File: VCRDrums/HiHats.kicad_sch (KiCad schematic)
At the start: 107 parts, among them Q601 BC847, Q602 BC857, Q603 BC847, Q604 BC857, Q605 BC847, Q606 BC847, Q607 BC847, Q608 BC847, Q609 BC847, Q610 BC847, Q611 BC847, Q612 BC847, Q613 BC847, Q614 BC847, Q615 BC857, U601 TL074, U602 LM13700

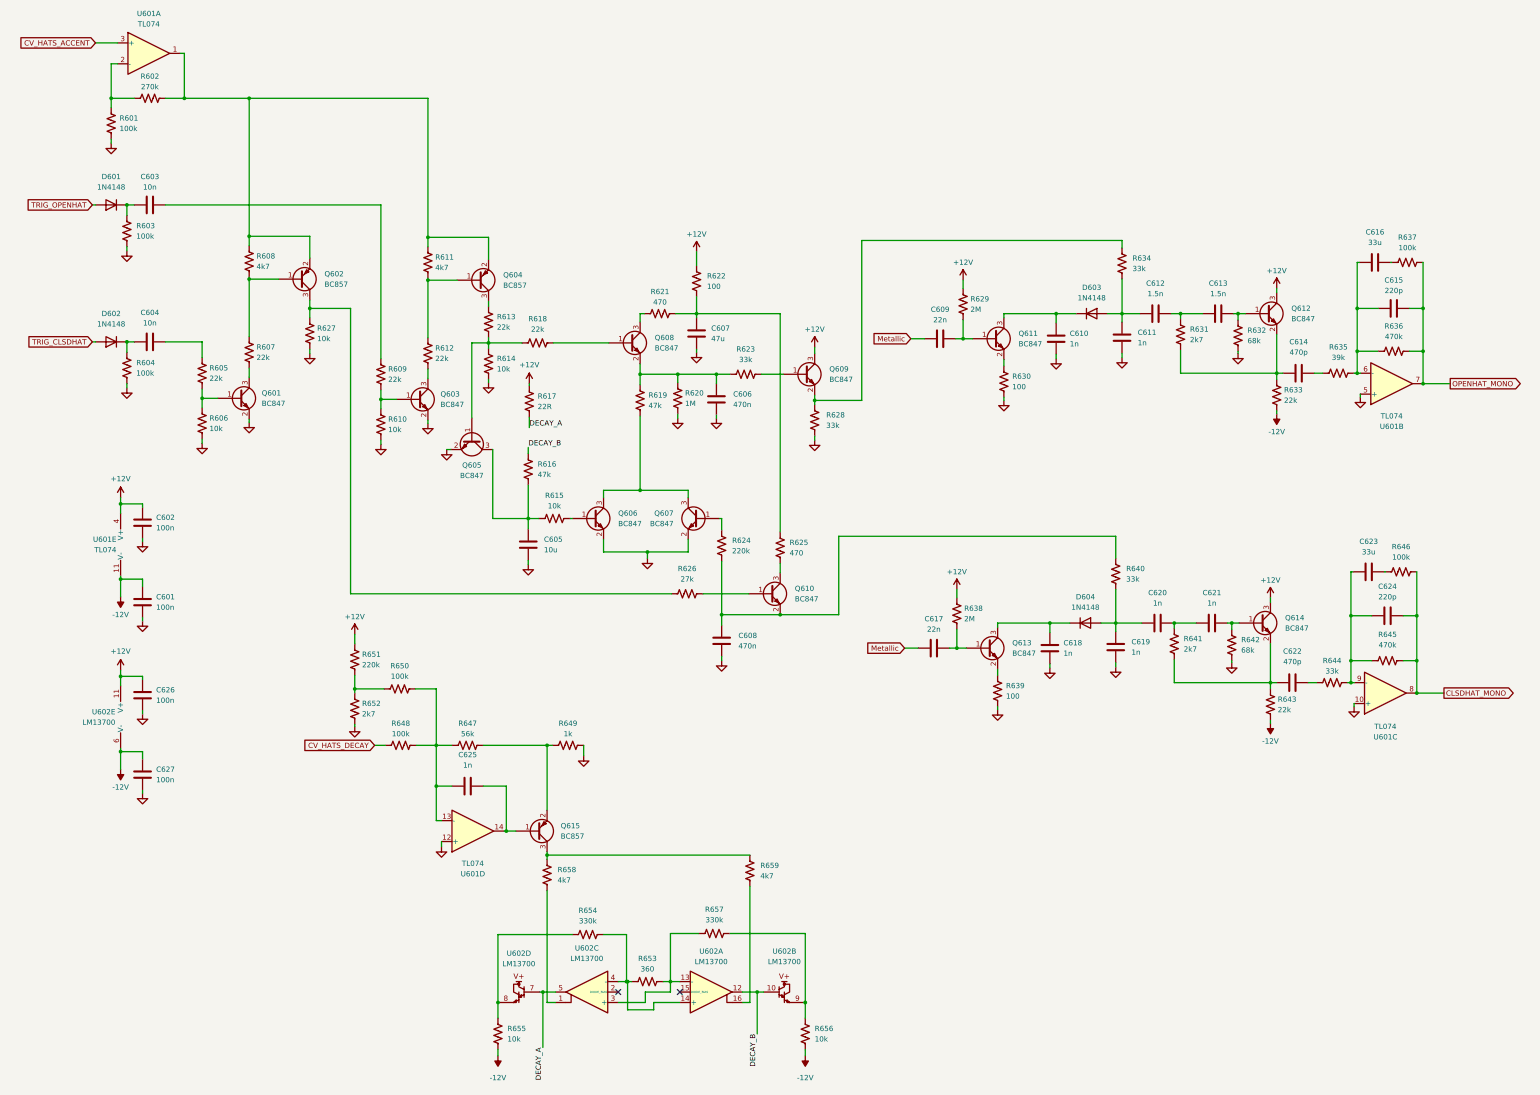
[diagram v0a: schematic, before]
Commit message: mcu skeleton
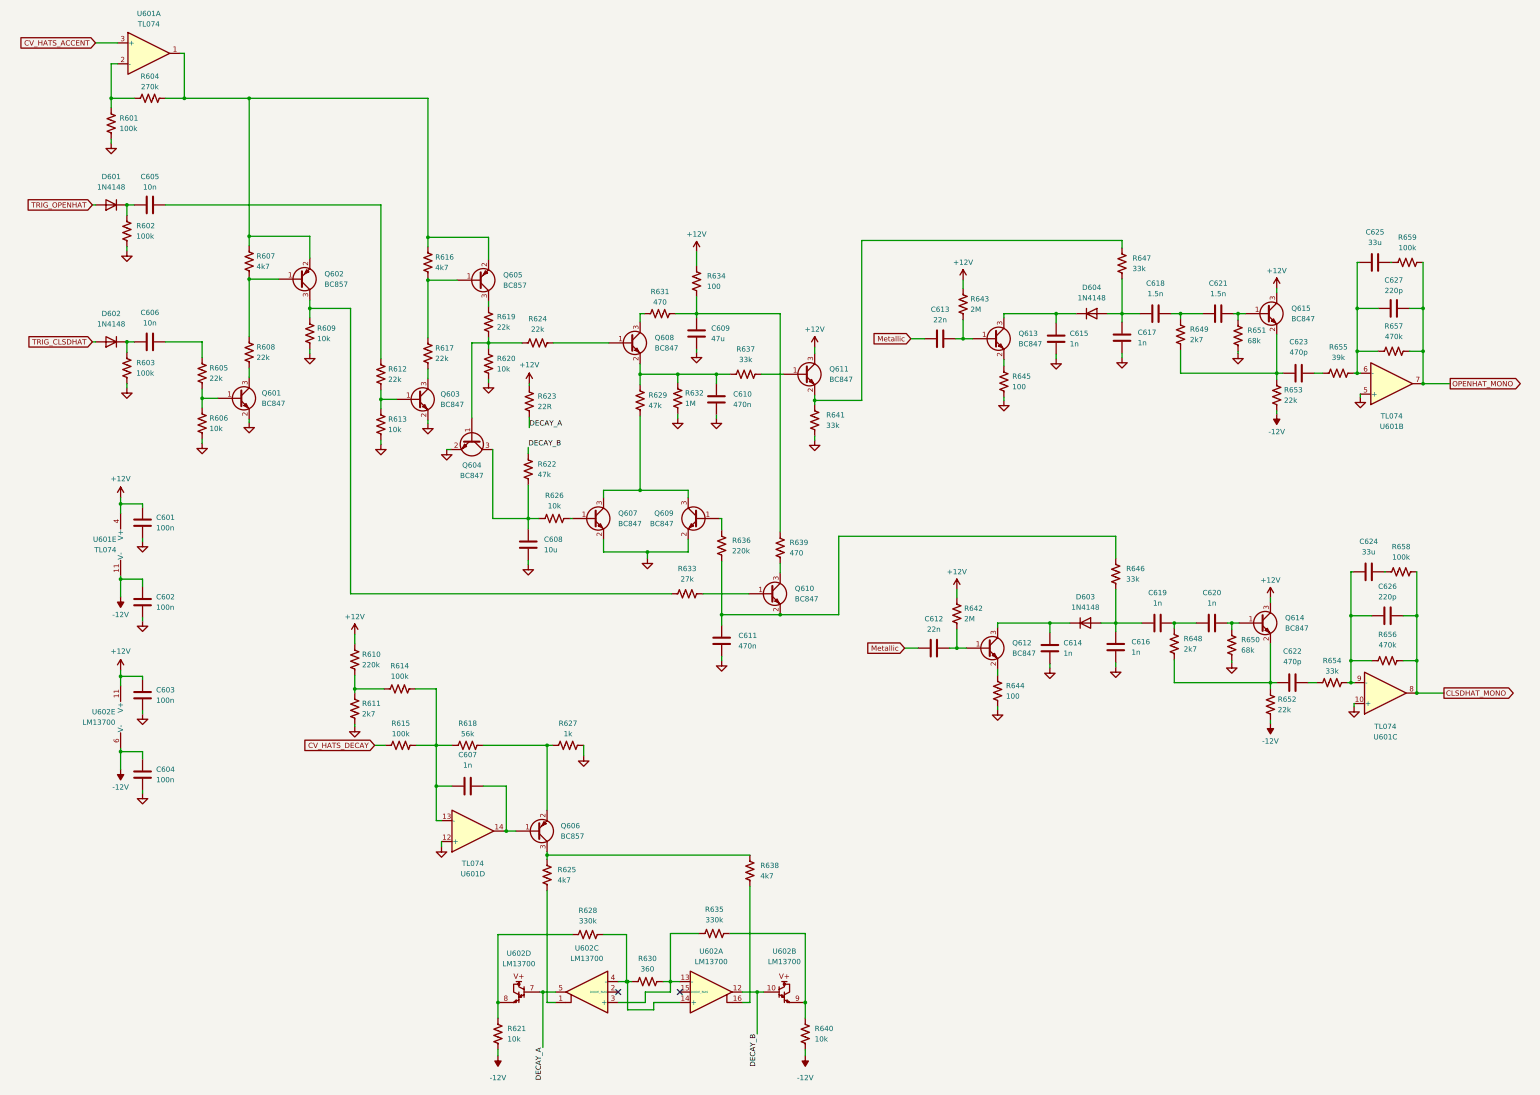
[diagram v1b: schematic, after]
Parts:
- C601: renamed from C602; footprint (none) -> Capacitor_SMD:C_0805_2012Metric
- C602: renamed from C601; footprint (none) -> Capacitor_SMD:C_0805_2012Metric
- C603: renamed from C626; footprint (none) -> Capacitor_SMD:C_0805_2012Metric
- C604: renamed from C627; footprint (none) -> Capacitor_SMD:C_0805_2012Metric
- C605: renamed from C603; footprint (none) -> Capacitor_SMD:C_0805_2012Metric
- C606: renamed from C604; footprint (none) -> Capacitor_SMD:C_0805_2012Metric
- C607: renamed from C625; footprint (none) -> Capacitor_SMD:C_0805_2012Metric
- C608: renamed from C605; footprint (none) -> Capacitor_SMD:C_0805_2012Metric
- C609: renamed from C607; footprint (none) -> Capacitor_SMD:C_0805_2012Metric
- C610: renamed from C606; footprint (none) -> Capacitor_SMD:C_0805_2012Metric
- C611: renamed from C608; footprint (none) -> Capacitor_SMD:C_0805_2012Metric
- C612: renamed from C617; footprint (none) -> Capacitor_SMD:C_0805_2012Metric
- C613: renamed from C609; footprint (none) -> Capacitor_SMD:C_0805_2012Metric
- C614: renamed from C618; footprint (none) -> Capacitor_SMD:C_0805_2012Metric
- C615: renamed from C610; footprint (none) -> Capacitor_SMD:C_0805_2012Metric
- C616: renamed from C619; footprint (none) -> Capacitor_SMD:C_0805_2012Metric
- C617: renamed from C611; footprint (none) -> Capacitor_SMD:C_0805_2012Metric
- C618: renamed from C612; footprint (none) -> Capacitor_SMD:C_0805_2012Metric
- C619: renamed from C620; footprint (none) -> Capacitor_SMD:C_0805_2012Metric
- C620: renamed from C621; footprint (none) -> Capacitor_SMD:C_0805_2012Metric
- C621: renamed from C613; footprint (none) -> Capacitor_SMD:C_0805_2012Metric
- C622: footprint (none) -> Capacitor_SMD:C_0805_2012Metric
- C623: renamed from C614; footprint (none) -> Capacitor_SMD:C_0805_2012Metric
- C624: renamed from C623; footprint (none) -> Capacitor_SMD:C_0805_2012Metric
- C625: renamed from C616; footprint (none) -> Capacitor_SMD:C_0805_2012Metric
- C626: renamed from C624; footprint (none) -> Capacitor_SMD:C_0805_2012Metric
- C627: renamed from C615; footprint (none) -> Capacitor_SMD:C_0805_2012Metric
- R601, R605, R606: footprint (none) -> Resistor_SMD:R_0805_2012Metric
- R602: renamed from R603; footprint (none) -> Resistor_SMD:R_0805_2012Metric
- R603: renamed from R604; footprint (none) -> Resistor_SMD:R_0805_2012Metric
- R604: renamed from R602; footprint (none) -> Resistor_SMD:R_0805_2012Metric
- R607: renamed from R608; footprint (none) -> Resistor_SMD:R_0805_2012Metric
- R608: renamed from R607; footprint (none) -> Resistor_SMD:R_0805_2012Metric
- R609: renamed from R627; footprint (none) -> Resistor_SMD:R_0805_2012Metric
- R610: renamed from R651; footprint (none) -> Resistor_SMD:R_0805_2012Metric
- R611: renamed from R652; footprint (none) -> Resistor_SMD:R_0805_2012Metric
- R612: renamed from R609; footprint (none) -> Resistor_SMD:R_0805_2012Metric
- R613: renamed from R610; footprint (none) -> Resistor_SMD:R_0805_2012Metric
- R614: renamed from R650; footprint (none) -> Resistor_SMD:R_0805_2012Metric
- R615: renamed from R648; footprint (none) -> Resistor_SMD:R_0805_2012Metric
- R616: renamed from R611; footprint (none) -> Resistor_SMD:R_0805_2012Metric
- R617: renamed from R612; footprint (none) -> Resistor_SMD:R_0805_2012Metric
- R618: renamed from R647; footprint (none) -> Resistor_SMD:R_0805_2012Metric
- R619: renamed from R613; footprint (none) -> Resistor_SMD:R_0805_2012Metric
- R620: renamed from R614; footprint (none) -> Resistor_SMD:R_0805_2012Metric
- R621: renamed from R655; footprint (none) -> Resistor_SMD:R_0805_2012Metric
- R622: renamed from R616; footprint (none) -> Resistor_SMD:R_0805_2012Metric
- R623: renamed from R617; footprint (none) -> Resistor_SMD:R_0805_2012Metric
- R624: renamed from R618; footprint (none) -> Resistor_SMD:R_0805_2012Metric
- R625: renamed from R658; footprint (none) -> Resistor_SMD:R_0805_2012Metric
- R626: renamed from R615; footprint (none) -> Resistor_SMD:R_0805_2012Metric
- R627: renamed from R649; footprint (none) -> Resistor_SMD:R_0805_2012Metric
- R628: renamed from R654; footprint (none) -> Resistor_SMD:R_0805_2012Metric
- R629: renamed from R619; footprint (none) -> Resistor_SMD:R_0805_2012Metric
- R630: renamed from R653; footprint (none) -> Resistor_SMD:R_0805_2012Metric
- R631: renamed from R621; footprint (none) -> Resistor_SMD:R_0805_2012Metric
- R632: renamed from R620; footprint (none) -> Resistor_SMD:R_0805_2012Metric
- R633: renamed from R626; footprint (none) -> Resistor_SMD:R_0805_2012Metric
- R634: renamed from R622; footprint (none) -> Resistor_SMD:R_0805_2012Metric
- R635: renamed from R657; footprint (none) -> Resistor_SMD:R_0805_2012Metric
- R636: renamed from R624; footprint (none) -> Resistor_SMD:R_0805_2012Metric
- R637: renamed from R623; footprint (none) -> Resistor_SMD:R_0805_2012Metric
- R638: renamed from R659; footprint (none) -> Resistor_SMD:R_0805_2012Metric
- R639: renamed from R625; footprint (none) -> Resistor_SMD:R_0805_2012Metric
- R640: renamed from R656; footprint (none) -> Resistor_SMD:R_0805_2012Metric
- R641: renamed from R628; footprint (none) -> Resistor_SMD:R_0805_2012Metric
- R642: renamed from R638; footprint (none) -> Resistor_SMD:R_0805_2012Metric
- R643: renamed from R629; footprint (none) -> Resistor_SMD:R_0805_2012Metric
- R644: renamed from R639; footprint (none) -> Resistor_SMD:R_0805_2012Metric
- R645: renamed from R630; footprint (none) -> Resistor_SMD:R_0805_2012Metric
- R646: renamed from R640; footprint (none) -> Resistor_SMD:R_0805_2012Metric
- R647: renamed from R634; footprint (none) -> Resistor_SMD:R_0805_2012Metric
- R648: renamed from R641; footprint (none) -> Resistor_SMD:R_0805_2012Metric
- R649: renamed from R631; footprint (none) -> Resistor_SMD:R_0805_2012Metric
- R650: renamed from R642; footprint (none) -> Resistor_SMD:R_0805_2012Metric
- R651: renamed from R632; footprint (none) -> Resistor_SMD:R_0805_2012Metric
- R652: renamed from R643; footprint (none) -> Resistor_SMD:R_0805_2012Metric
- R653: renamed from R633; footprint (none) -> Resistor_SMD:R_0805_2012Metric
- R654: renamed from R644; footprint (none) -> Resistor_SMD:R_0805_2012Metric
- R655: renamed from R635; footprint (none) -> Resistor_SMD:R_0805_2012Metric
- R656: renamed from R645; footprint (none) -> Resistor_SMD:R_0805_2012Metric
- R657: renamed from R636; footprint (none) -> Resistor_SMD:R_0805_2012Metric
- R658: renamed from R646; footprint (none) -> Resistor_SMD:R_0805_2012Metric
- R659: renamed from R637; footprint (none) -> Resistor_SMD:R_0805_2012Metric
- U601: footprint (none) -> Package_SO:SOIC-14_3.9x8.7mm_P1.27mm
- U602: footprint (none) -> Package_SO:SOIC-16_3.9x9.9mm_P1.27mm
- renumbered D604 to D603, D603 to D604, Q605 to Q604, Q604 to Q605, Q615 to Q606, Q606 to Q607, Q607 to Q609, Q609 to Q611, Q613 to Q612, Q611 to Q613, Q612 to Q615

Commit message: compressor schem and schematic
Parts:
- D601, D602, D603, D604: footprint Diode_THT:D_DO-35_SOD27_P7.62mm_Horizontal -> Diode_SMD:D_SOD-123
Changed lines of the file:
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@@
 			)
 		)
-		(property "Footprint" "Diode_THT:D_DO-35_SOD27_P7.62mm_Horizontal"
+		(property "Footprint" "Diode_SMD:D_SOD-123"
 			(at 42.418 98.806 0)
 			(effects
@@
 			)
 		)
-		(property "Footprint" "Diode_THT:D_DO-35_SOD27_P7.62mm_Horizontal"
+		(property "Footprint" "Diode_SMD:D_SOD-123"
 			(at 42.418 65.532 0)
 			(effects
@@
 			)
 		)
-		(property "Footprint" "Diode_THT:D_DO-35_SOD27_P7.62mm_Horizontal"
+		(property "Footprint" "Diode_SMD:D_SOD-123"
 			(at 279.146 167.132 0)
 			(effects
@@
 			)
 		)
-		(property "Footprint" "Diode_THT:D_DO-35_SOD27_P7.62mm_Horizontal"
+		(property "Footprint" "Diode_SMD:D_SOD-123"
 			(at 280.67 91.948 0)
 			(effects
